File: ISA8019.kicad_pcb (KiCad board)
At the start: 2 copper layers, 129.5 x 73.9 mm, 53 parts, among them J1 Bus_ISA_8bit, J2 8P8C_Shielded, J4 Jumper mode, J5 PNP force, J6 BROM size and base address, J7 I/O base address, J8 Medium type, J9 IRQ select, T1 13F-39MNL, U1 RTL8019AS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

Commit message: Fix bottom no-net fill
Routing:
- added copper zone on B.Cu, net GND
- removed copper zone on B.Cu, net (none)

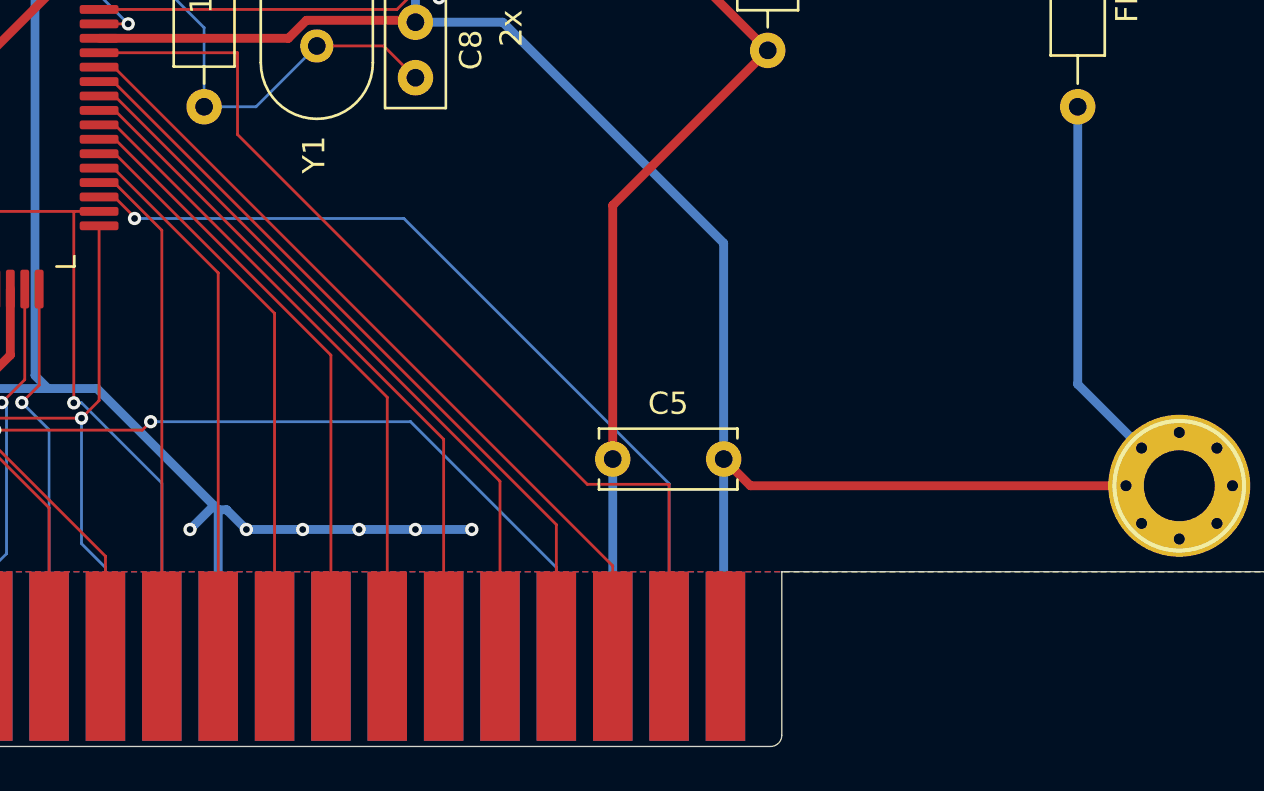
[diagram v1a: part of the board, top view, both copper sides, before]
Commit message: Add another filter cap
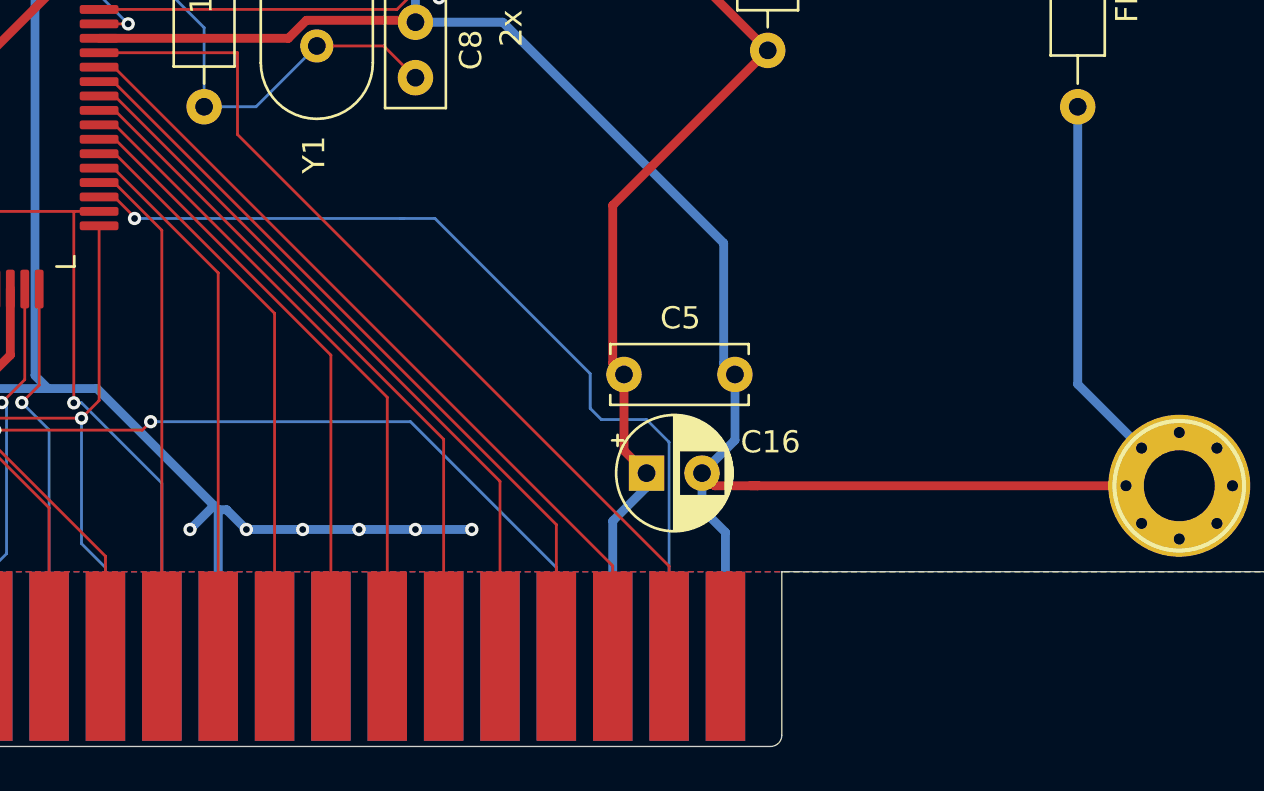
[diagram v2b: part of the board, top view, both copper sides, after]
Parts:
- added C16: 10uF, Capacitor_THT:CP_Radial_D5.0mm_P2.50mm, F.Cu at (164.1, 151.0)
- C2: value 47uF -> 10uF
- moved C5 3.84 mm to (163.1, 146.6)
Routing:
- net GND: track 545.4 -> 547.7 mm
- net /ISA_RESET: track 38.9 -> 41.0 mm
- net /ISA_D7: track 43.7 -> 41.5 mm
- net +5V: track 348.0 -> 349.3 mm

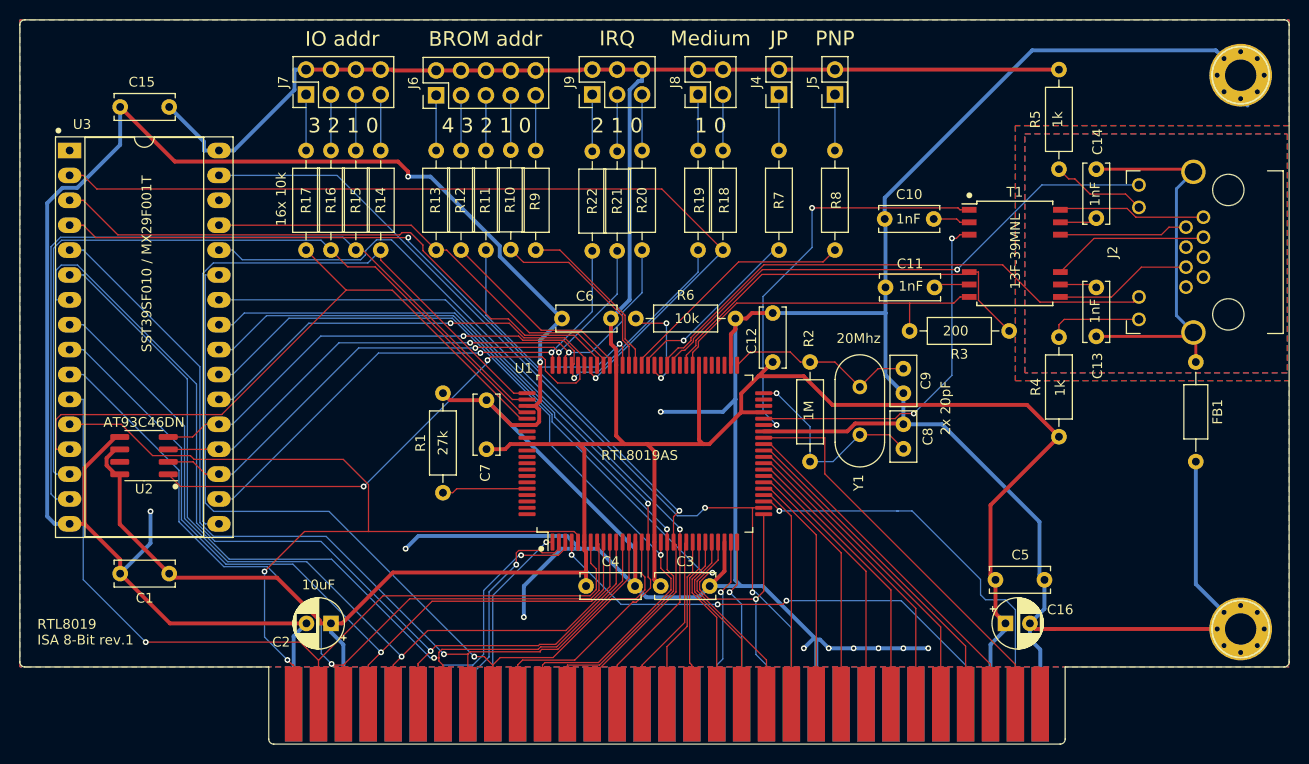
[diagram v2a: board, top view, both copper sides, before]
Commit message: Adjust board edges
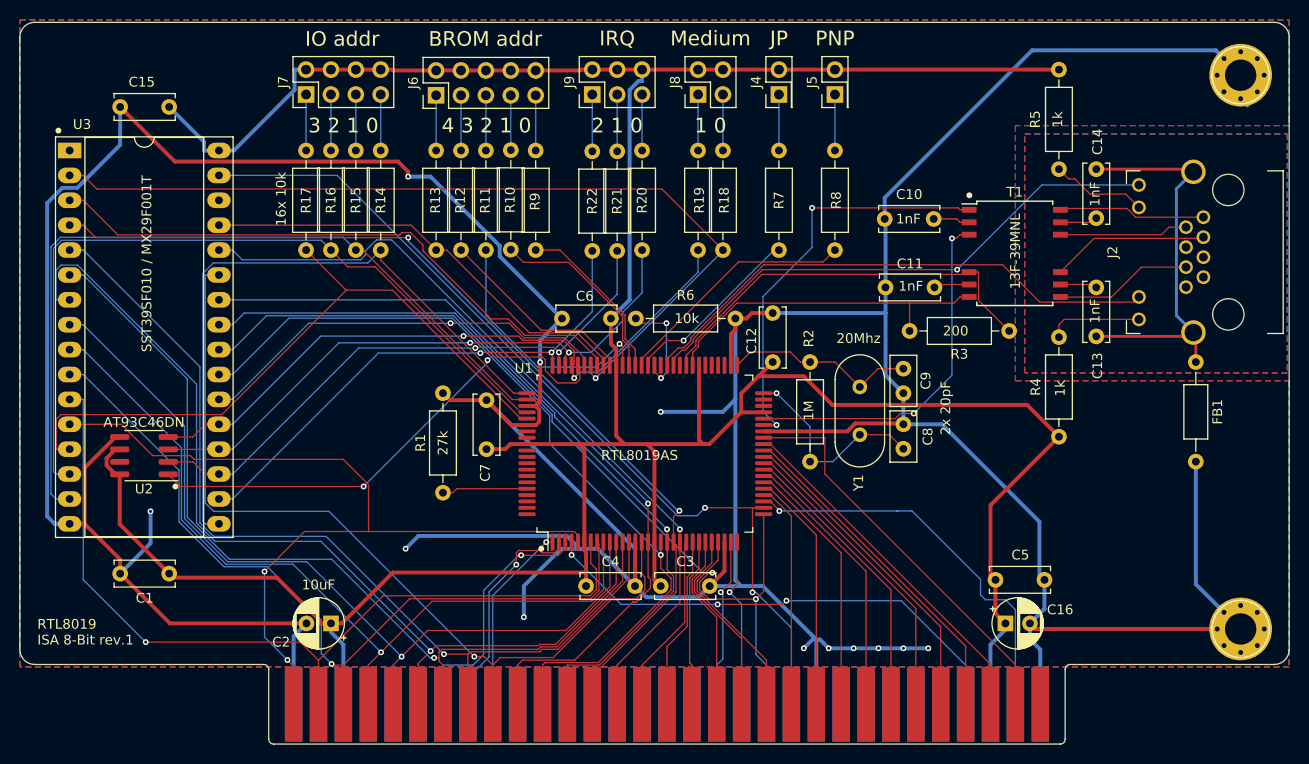
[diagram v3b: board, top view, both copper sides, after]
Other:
- board size 129.5 x 73.9 mm -> 129.5 x 73.7 mm
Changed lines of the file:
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@@
   (general
     (thickness 1.6)
-    (drawings 65)
+    (drawings 67)
     (tracks 955)
     (zones 0)
@@
   (page A4)
   (layers
-    (0 F.Cu signal hide)
-    (31 B.Cu signal hide)
+    (0 F.Cu signal)
+    (31 B.Cu signal)
     (32 B.Adhes user)
-    (33 F.Adhes user hide)
+    (33 F.Adhes user)
     (34 B.Paste user)
     (35 F.Paste user)
@@
     )
   )
+  (gr_arc (start 65.084 153.712) (end 63.56 153.712) (angle -90) (layer Edge.Cuts) (width 0.05))
+  (gr_arc (start 88.452 155.744) (end 88.96 155.744) (angle -90) (layer Edge.Cuts) (width 0.05))
+  (gr_arc (start 170.748 155.744) (end 170.748 155.236) (angle -90) (layer Edge.Cuts) (width 0.05))
+  (gr_arc (start 191.576 153.712) (end 191.576 155.236) (angle -90) (layer Edge.Cuts) (width 0.05))
+  (gr_arc (start 191.576 91.228) (end 193.1 91.228) (angle -90) (layer Edge.Cuts) (width 0.05))
+  (gr_arc (start 65.084 91.228) (end 65.084 89.704) (angle -90) (layer Edge.Cuts) (width 0.05))
   (gr_text "RTL8019\nISA 8-Bit rev.1" (at 65.338 151.934) (layer F.SilkS)
     (effects (font (size 1 1) (thickness 0.15)) (justify left))
@@
   (gr_line (start 93.532 99.102) (end 93.532 148.632) (layer B.SilkS) (width 0.12))
   (gr_line (start 169.732 163.364) (end 89.468 163.364) (layer Edge.Cuts) (width 0.05))
-  (gr_line (start 170.24 155.49) (end 170.24 162.856) (layer Edge.Cuts) (width 0.05))
-  (gr_line (start 192.592 155.49) (end 170.24 155.49) (layer Edge.Cuts) (width 0.05))
-  (gr_line (start 193.1 89.958) (end 193.1 154.982) (layer Edge.Cuts) (width 0.05))
-  (gr_line (start 64.068 89.45) (end 192.592 89.45) (layer Edge.Cuts) (width 0.05))
-  (gr_line (start 63.56 154.982) (end 63.56 89.958) (layer Edge.Cuts) (width 0.05))
-  (gr_line (start 88.96 155.49) (end 64.068 155.49) (layer Edge.Cuts) (width 0.05))
-  (gr_line (start 88.96 162.856) (end 88.96 155.49) (layer Edge.Cuts) (width 0.05))
+  (gr_line (start 170.24 155.744) (end 170.24 162.856) (layer Edge.Cuts) (width 0.05))
+  (gr_line (start 191.576 155.236) (end 170.748 155.236) (layer Edge.Cuts) (width 0.05))
+  (gr_line (start 193.1 91.228) (end 193.1 153.712) (layer Edge.Cuts) (width 0.05))
+  (gr_line (start 65.084 89.704) (end 191.576 89.704) (layer Edge.Cuts) (width 0.05))
+  (gr_line (start 63.56 153.712) (end 63.56 91.228) (layer Edge.Cuts) (width 0.05))
+  (gr_line (start 88.452 155.236) (end 65.084 155.236) (layer Edge.Cuts) (width 0.05))
+  (gr_line (start 88.96 162.856) (end 88.96 155.744) (layer Edge.Cuts) (width 0.05))
   (gr_arc (start 89.468 162.856) (end 88.96 162.856) (angle -90) (layer Edge.Cuts) (width 0.05))
   (gr_arc (start 169.732 162.856) (end 169.732 163.364) (angle -90) (layer Edge.Cuts) (width 0.05))
-  (gr_arc (start 192.592 154.982) (end 192.592 155.49) (angle -90) (layer Edge.Cuts) (width 0.05))
-  (gr_arc (start 192.592 89.958) (end 193.1 89.958) (angle -90) (layer Edge.Cuts) (width 0.05))
-  (gr_arc (start 64.068 89.958) (end 64.068 89.45) (angle -90) (layer Edge.Cuts) (width 0.05))
-  (gr_arc (start 64.068 154.982) (end 63.56 154.982) (angle -90) (layer Edge.Cuts) (width 0.05))
   (gr_text 200 (at 159.064 121.2) (layer F.SilkS)
     (effects (font (size 1 1) (thickness 0.15)))

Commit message: Update the revision
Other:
- board text added: "RTL8019 ISA 8-Bit rev.2"
- board text removed: "RTL8019 ISA 8-Bit rev.1"
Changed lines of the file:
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@@
   (page A4)
   (layers
-    (0 F.Cu signal)
-    (31 B.Cu signal)
+    (0 F.Cu signal hide)
+    (31 B.Cu signal hide)
     (32 B.Adhes user)
     (33 F.Adhes user)
@@
   (gr_arc (start 191.576 91.228) (end 193.1 91.228) (angle -90) (layer Edge.Cuts) (width 0.05))
   (gr_arc (start 65.084 91.228) (end 65.084 89.704) (angle -90) (layer Edge.Cuts) (width 0.05))
-  (gr_text "RTL8019\nISA 8-Bit rev.1" (at 65.338 151.934) (layer F.SilkS)
+  (gr_text "RTL8019\nISA 8-Bit rev.2" (at 65.338 151.934) (layer F.SilkS)
     (effects (font (size 1 1) (thickness 0.15)) (justify left))
   )

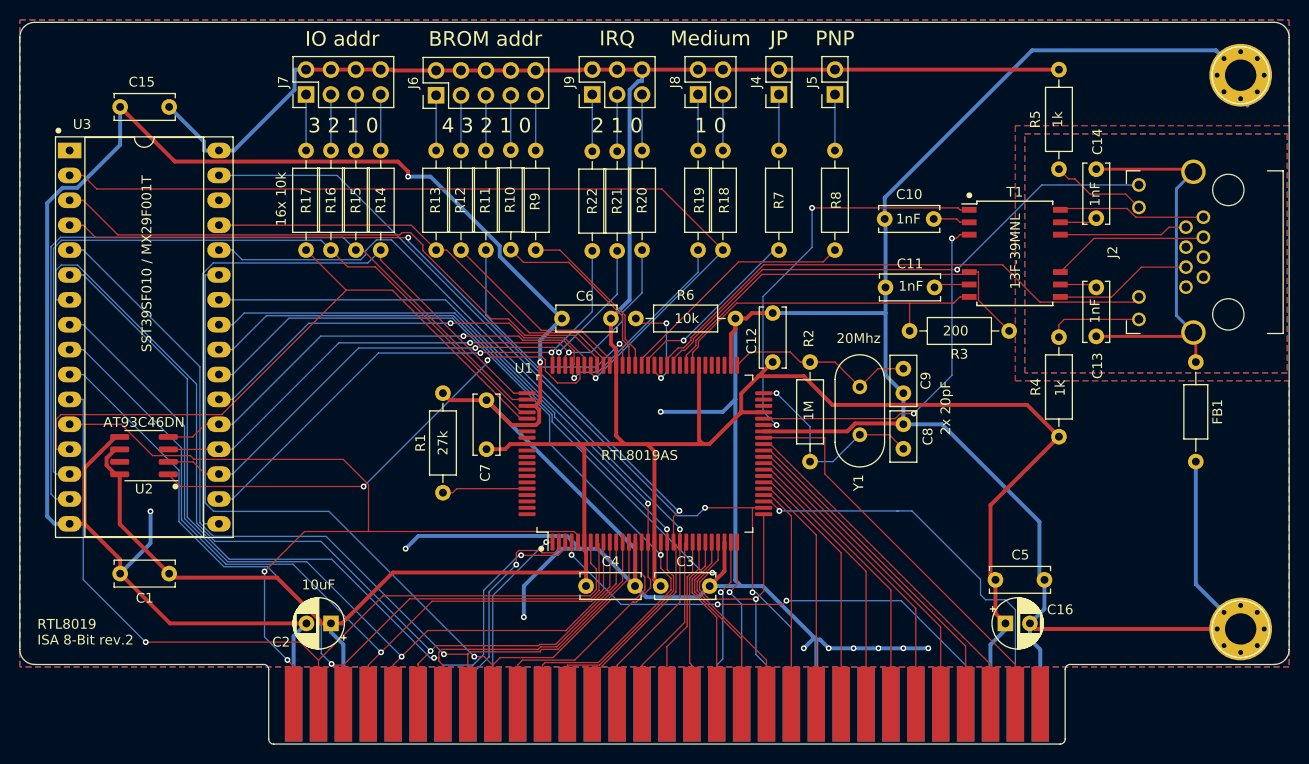
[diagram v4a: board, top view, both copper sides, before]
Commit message: Resize board and remove jumper for 16-bit IRQs
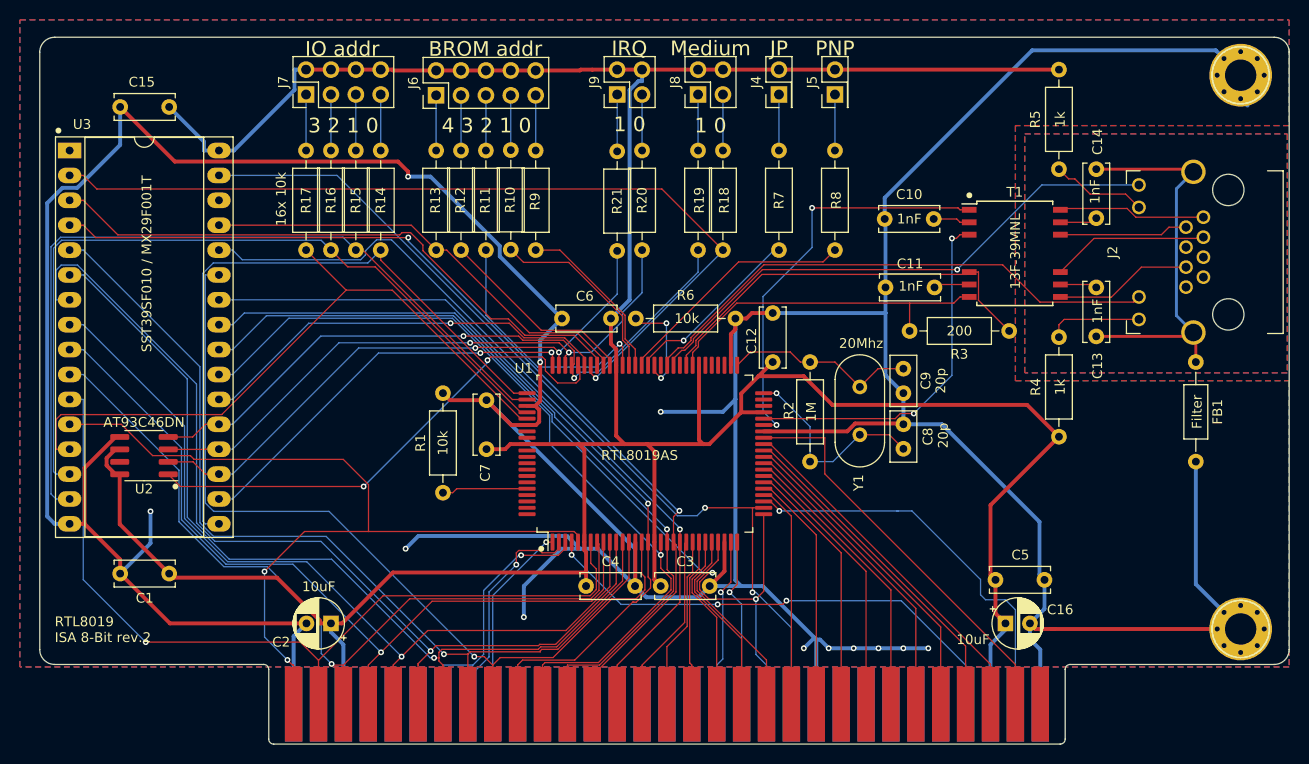
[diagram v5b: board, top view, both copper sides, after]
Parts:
- removed R22: 10k, Resistor_THT:R_Axial_DIN0207_L6.3mm_D2.5mm_P10.16mm_Horizontal
- FB1: value Ferrite_Bead -> Filter
- J9: footprint Connector_PinHeader_2.54mm:PinHeader_2x03_P2.54mm_Vertical -> Connector_PinHeader_2.54mm:PinHeader_2x02_P2.54mm_Vertical
- R1: value 27k -> 10k
- R3: value 200R -> 200
- moved J9 2.54 mm to (124.5, 97.1)
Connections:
- R20 pad 2: Net-(J9-Pad5) -> Net-(J9-Pad3)
- R21 pad 2: Net-(J9-Pad3) -> Net-(J9-Pad1)
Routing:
- net /BD4: track 53.6 -> 41.5 mm
- net Net-(J9-Pad5): track 5.72 -> 0.00 mm
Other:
- board size 129.5 x 73.7 mm -> 127.5 x 72.1 mm
- board text added: "IRQ 1 0 0 0 IRQ2 0 1 IRQ3 1 0 IRQ4 1 1 IRQ5"
- board text removed: "10k"
- board text removed: "10uF"
- board text removed: "1M"
- board text removed: "1k"
- board text removed: "2 1 0"
- board text removed: "200"
- board text removed: "20Mhz"
- board text removed: "27k"
- board text removed: "2x 20pF"
- board text removed: "IRQ 2 1 0 0 0 0 IRQ2 0 0 1 IRQ3 0 1 0 IRQ4 0 1 1 IRQ5 1 0 0 IRQ10 1 0 1 IRQ11 1 1 0 IRQ12 1 1 1 IRQ15"

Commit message: Removed useless pulldown resistor
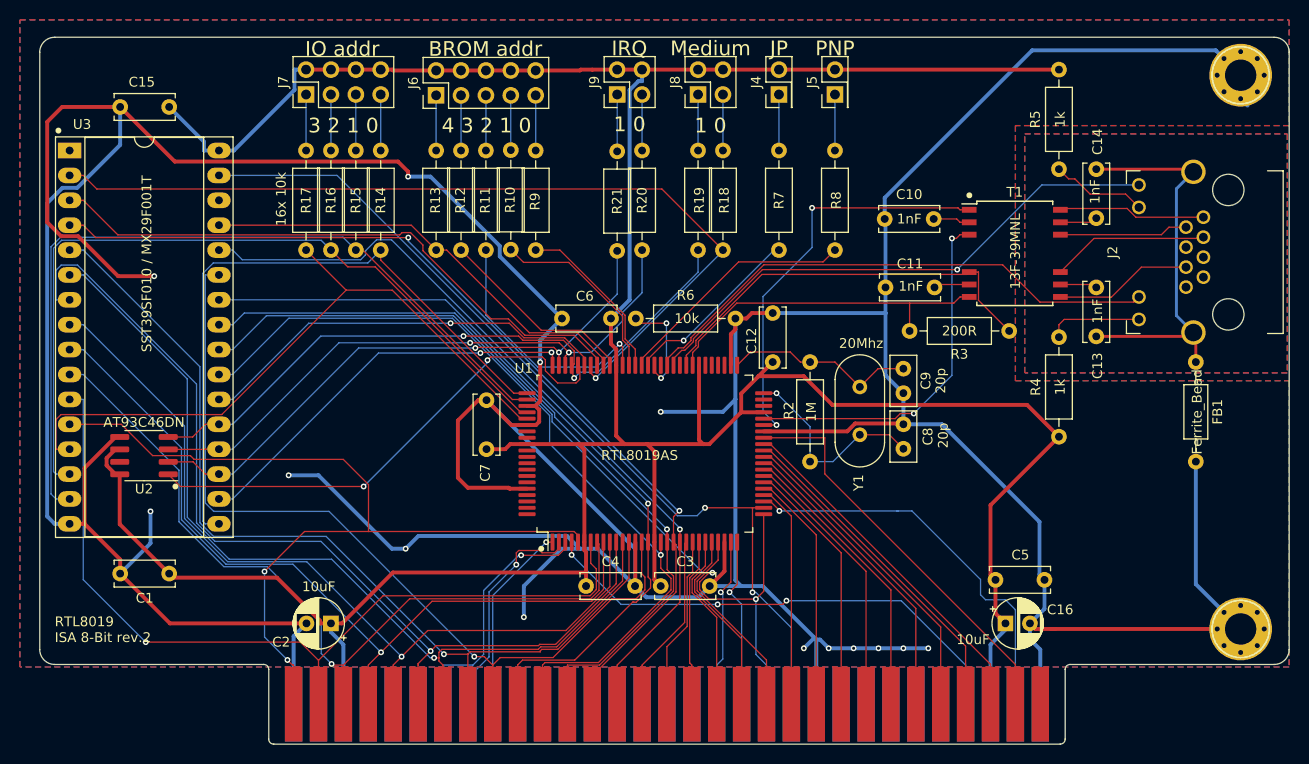
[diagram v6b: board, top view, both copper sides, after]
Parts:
- removed R1: 10k, Resistor_THT:R_Axial_DIN0207_L6.3mm_D2.5mm_P10.16mm_Horizontal
- FB1: value Filter -> Ferrite_Bead
- R3: value 200 -> 200R
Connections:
- U1 pad 96: /~ISA_IOCS16 -> GND
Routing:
- net GND: track 547.7 -> 606.7 mm, vias 12 -> 14
- net /~ISA_IOCS16: track 8.75 -> 0.00 mm
